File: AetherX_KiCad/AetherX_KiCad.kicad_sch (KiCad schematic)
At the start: 17 parts, among them J1 SWD Connector, SW1 SW_SPDT, U1 STM32F401RETx, Y1 8MHz

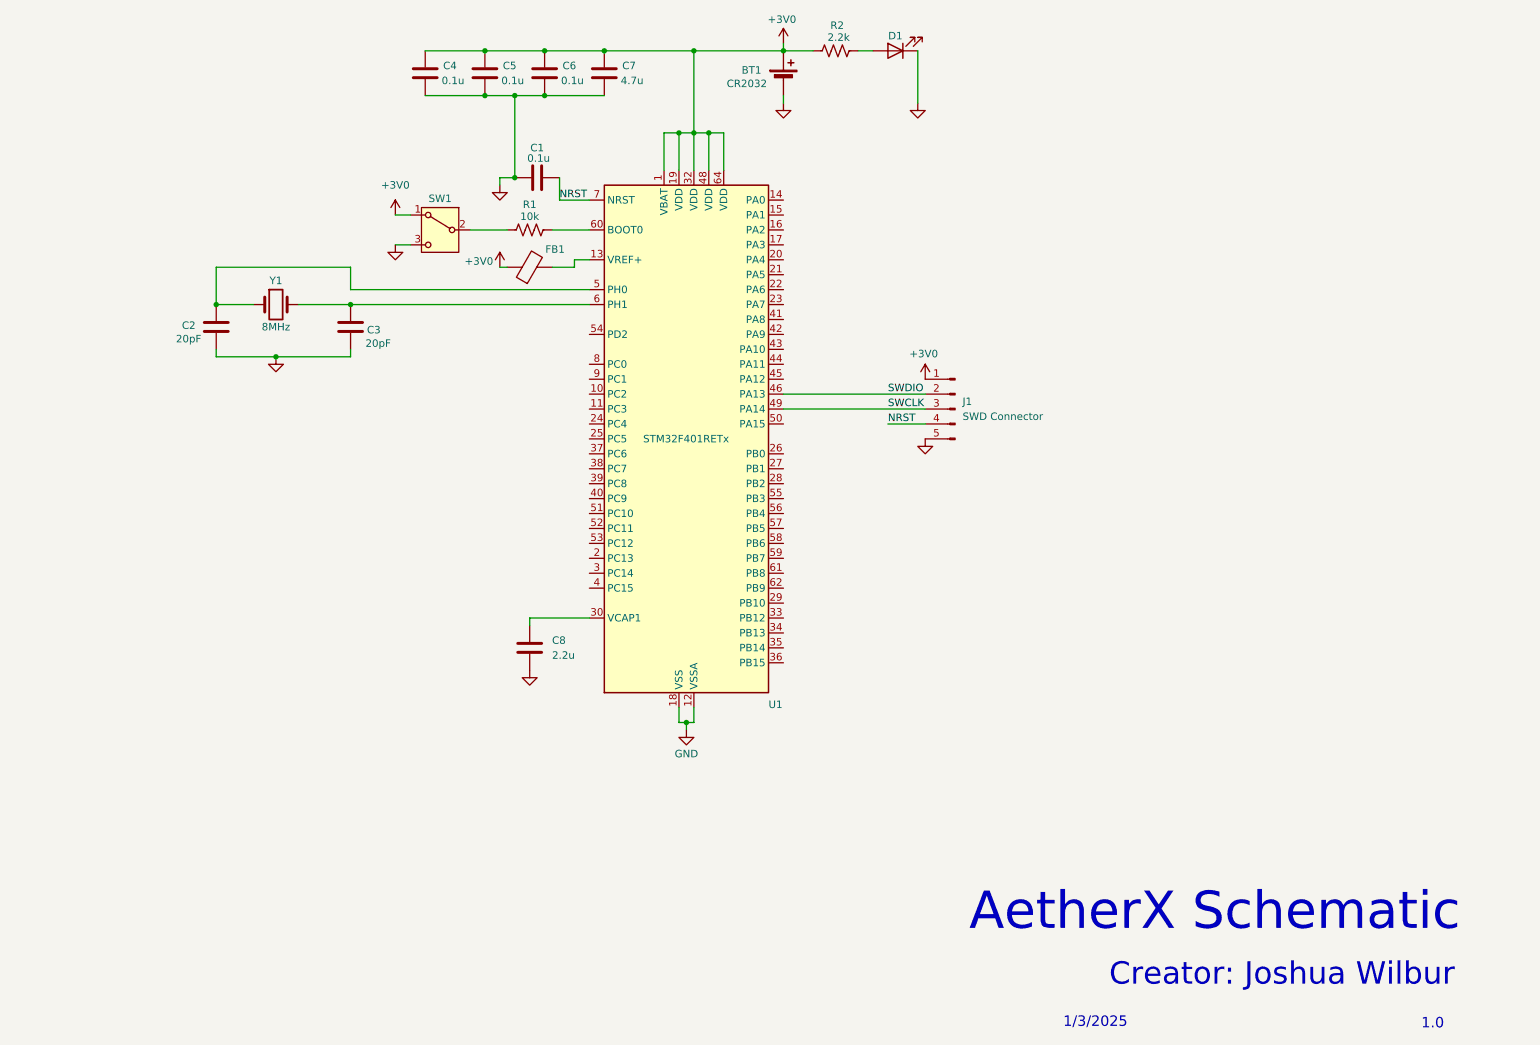
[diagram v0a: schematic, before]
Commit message: update schematic
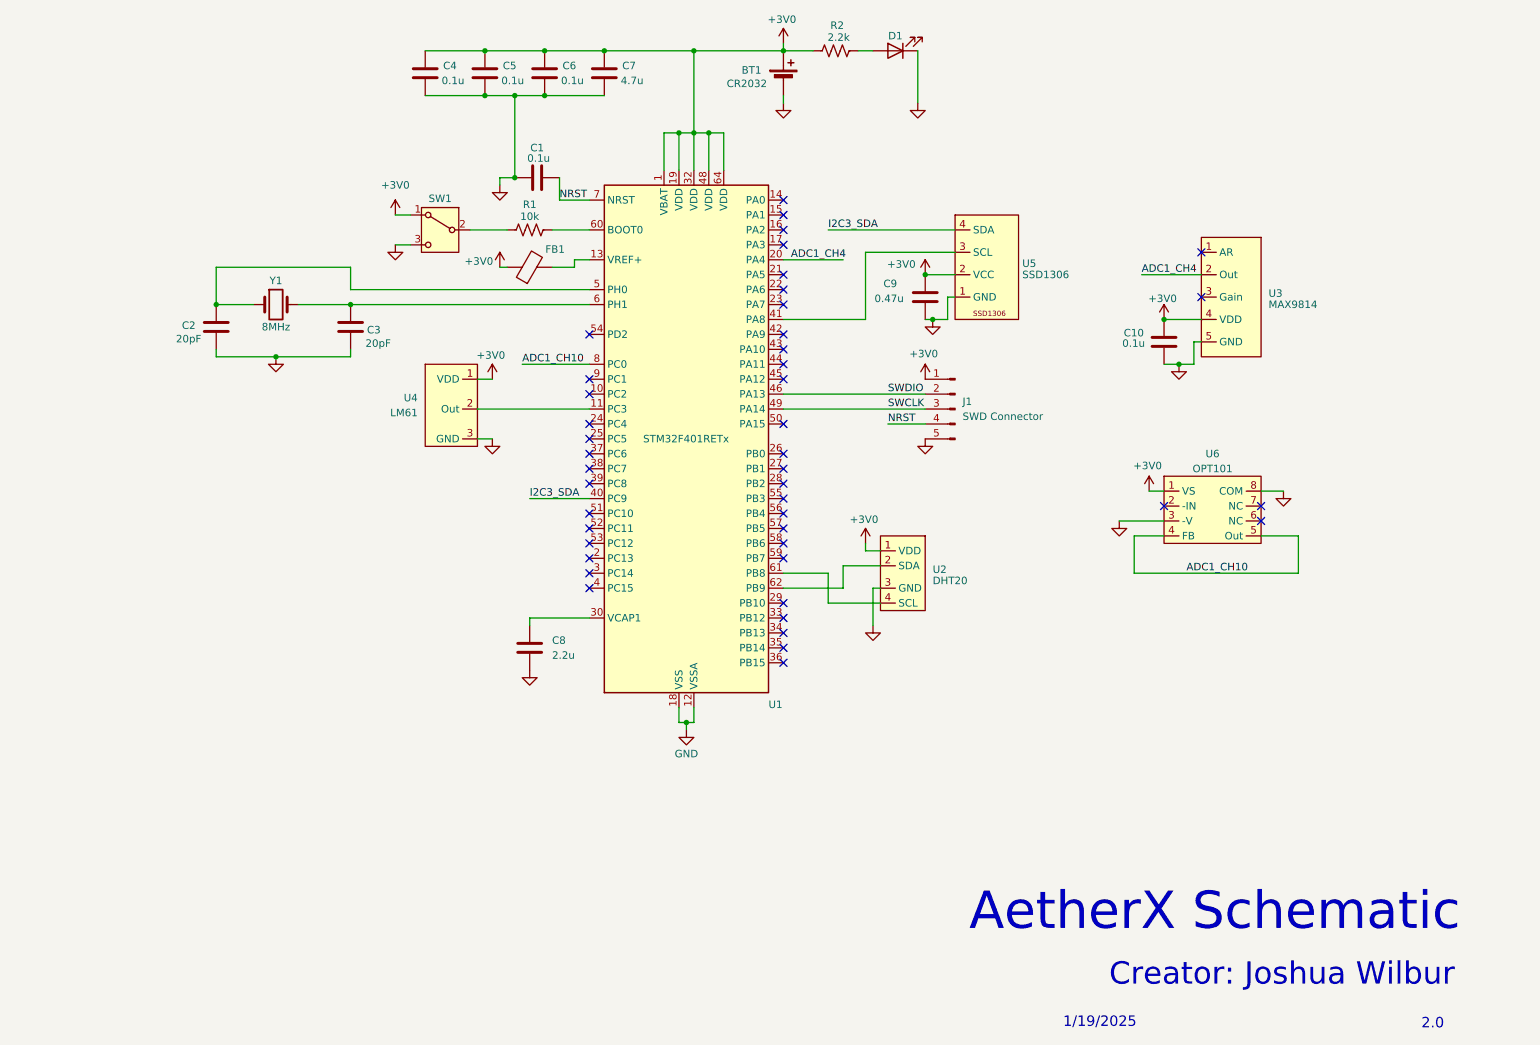
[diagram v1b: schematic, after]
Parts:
- added C10: 0.1u, symbol Device:C
- added C9: 0.47u, symbol Device:C
- added U2: DHT20, symbol Device:DHT20
- added U3: MAX9814, symbol Device:MAX9814
- added U4: LM61, symbol Device:LM61
- added U5: SSD1306, symbol Device:SSD1306_LCD
- added U6: OPT101, symbol Device:OPT101
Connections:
- net +3V0: now also C10.1, C9.1, U2.1 (VDD), U3.4 (VDD), U4.1 (VDD), U5.2 (VCC), U6.1 (VS)
- net GND: now also C10.2, C9.2, U2.3 (GND), U3.5 (GND), U4.3 (GND), U5.1 (GND), U6.3 (-V), U6.8 (COM)
- net at U1.11 (PC3): now also U4.2 (Out)
- net ADC1_CH4: now reaches U1.20 (PA4)
- net ADC1_CH4: now also U3.2 (Out)
- net I2C3_SDA: now reaches U1.40 (PC9)
- net I2C3_SDA: now also U5.4 (SDA)
- net at U1.41 (PA8): now also U5.3 (SCL)
- net at U1.61 (PB8): now also U2.4 (SCL)
- net at U1.62 (PB9): now also U2.2 (SDA)
- net ADC1_CH10: now reaches U1.8 (PC0)
- net ADC1_CH10: now also U6.4 (FB), U6.5 (Out)
- no-connect marks 0 -> 44
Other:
- note added: "1/19/2025"
- note added: "2.0"
- note removed: "1.0"
- note removed: "1/3/2025"

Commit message: internal ADC VRef code added
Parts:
- added C11, C12: 0.1u, symbol Device:C
- added R3, R5: 1k, symbol Device:R_US
- added R4, R6: 10k, symbol Device:R_US
- added SW2, SW3: SW_Push, symbol Switch:SW_Push
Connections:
- net +3V0: now also R4.1, R6.1
- net GND: now also C11.2, C12.2, SW2.1, SW3.1
- net Button1: now reaches U1.24 (PC4)
- net Button1: now also C11.1, R3.2, R4.2
- net Button2: now reaches U1.25 (PC5)
- net Button2: now also C12.1, R5.2, R6.2
- new net: R5.1, SW3.2
- new net: R3.1, SW2.2
- no-connect marks 44 -> 42

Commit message: schematic V2 complete
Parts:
- added C13: 0.1u, Capacitor_SMD:C_0402_1005Metric_Pad0.74x0.62mm_HandSolder, symbol Device:C
- BT1: footprint (none) -> Battery:BatteryHolder_Keystone_103_1x20mm; now left out of the parts list
- C1, C2, C3, Y1: now left out of the parts list
- C10, C11, C12: footprint (none) -> Capacitor_SMD:C_0402_1005Metric_Pad0.74x0.62mm_HandSolder
- C8, C9: footprint (none) -> Capacitor_THT:C_Disc_D5.1mm_W3.2mm_P5.00mm; now left out of the parts list
- D1: footprint (none) -> LED_THT:LED_D5.0mm; now left out of the parts list
- FB1: footprint (none) -> Inductor_THT:L_Axial_L7.0mm_D3.3mm_P12.70mm_Horizontal_Fastron_MICC
- J1, U3: footprint (none) -> Connector_PinSocket_2.54mm:PinSocket_1x05_P2.54mm_Vertical; now left out of the parts list
- R1, R2, R4, R6: footprint (none) -> Resistor_THT:R_Axial_DIN0207_L6.3mm_D2.5mm_P10.16mm_Horizontal; now left out of the parts list
- R3, R5: footprint (none) -> Resistor_THT:R_Axial_DIN0207_L6.3mm_D2.5mm_P10.16mm_Horizontal
- SW1, U4: footprint (none) -> Connector_PinHeader_2.54mm:PinHeader_1x03_P2.54mm_Vertical; now left out of the parts list
- SW2, SW3: footprint (none) -> Button_Switch_THT:SW_PUSH_1P1T_6x3.5mm_H5.0_APEM_MJTP1250; now left out of the parts list
- U2, U5: footprint (none) -> Connector_PinSocket_2.54mm:PinSocket_1x04_P2.54mm_Vertical; now left out of the parts list
- U6: footprint (none) -> Package_DIP:DIP-8_W7.62mm; now left out of the parts list
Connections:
- net +3V0: now also C13.1
- net GND: now also C13.2
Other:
- note added: "1/30/2025"
- note added: "2.2"
- note removed: "1/19/2025"
- note removed: "2.0"
- moved on the sheet: C11, C12, R3, R4, R5, R6, SW2, SW3

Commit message: first PCB complete
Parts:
- renumbered SW2 to SW1, SW3 to SW2, SW1 to SW_BOOT1
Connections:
- net +3V0: no longer R2.1
- net LED: now reaches U1.51 (PC10)
- net LED: now also R2.1
- no-connect marks 42 -> 41
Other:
- moved on the sheet: D1, R2
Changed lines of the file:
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@@
 	)
 	(no_connect
-		(at 127 106.68)
-	)
-	(no_connect
 		(at 160.02 101.6)
 	)
@@
 	(wire
 		(pts
-			(xy 160.02 27.94) (xy 165.1 27.94)
-		)
-		(stroke
-			(width 0)
-			(type default)
-		)
-	)
-	(wire
-		(pts
 			(xy 142.24 41.91) (xy 144.78 41.91)
 		)
@@
 	(wire
 		(pts
+			(xy 175.26 36.83) (xy 180.34 36.83)
+		)
+		(stroke
+			(width 0)
+			(type default)
+		)
+	)
+	(wire
+		(pts
 			(xy 120.65 58.42) (xy 127 58.42)
 		)
@@
 	(wire
 		(pts
-			(xy 172.72 27.94) (xy 175.26 27.94)
+			(xy 187.96 36.83) (xy 190.5 36.83)
 		)
 		(stroke
@@
 	(wire
 		(pts
+			(xy 116.84 106.68) (xy 127 106.68)
+		)
+		(stroke
+			(width 0)
+			(type default)
+		)
+	)
+	(wire
+		(pts
 			(xy 167.64 121.92) (xy 176.53 121.92)
 		)
@@
 	(wire
 		(pts
-			(xy 182.88 27.94) (xy 182.88 36.83)
+			(xy 198.12 36.83) (xy 198.12 45.72)
 		)
 		(stroke
@@
 		)
 	)
+	(label "LED"
+		(at 116.84 106.68 0)
+		(effects
+			(font
+				(size 1.27 1.27)
+			)
+			(justify left bottom)
+		)
+	)
 	(label "ADC1_CH4"
 		(at 161.29 63.5 0)
@@
 		)
 	)
+	(label "LED"
+		(at 175.26 36.83 0)
+		(effects
+			(font
+				(size 1.27 1.27)
+			)
+			(justify left bottom)
+		)
+	)
 	(label "SWDIO"
 		(at 177.8 86.36 0)
@@
 		(on_board yes)
 		(dnp no)
-		(property "Reference" "SW1"
+		(property "Reference" "SW_BOOT1"
 			(at 101.6 53.086 0)
 			(effects
@@
 			(project ""
 				(path "/e3a9a061-ed84-4419-81aa-dfe9405e0b6b"
-					(reference "SW1")
+					(reference "SW_BOOT1")
 					(unit 1)
 				)
@@
 	(symbol
 		(lib_id "power:GND")
-		(at 182.88 36.83 0)
+		(at 198.12 45.72 0)
 		(unit 1)
 		(exclude_from_sim no)
@@
 		(fields_autoplaced yes)
 		(property "Reference" "#PWR08"
-			(at 182.88 43.18 0)
+			(at 198.12 52.07 0)
 			(effects
 				(font
@@
 		)
 		(property "Value" "GND"
-			(at 182.88 41.91 0)
+			(at 198.12 50.8 0)
 			(effects
 				(font
@@
 		)
 		(property "Footprint" ""
-			(at 182.88 36.83 0)
+			(at 198.12 45.72 0)
 			(effects
 				(font
@@
 		)
 		(property "Datasheet" ""
-			(at 182.88 36.83 0)
+			(at 198.12 45.72 0)
 			(effects
 				(font
@@
 		)
 		(property "Description" "Power symbol creates a global label with name \"GND\" , ground"
-			(at 182.88 36.83 0)
+			(at 198.12 45.72 0)
 			(effects
 				(font
@@
 	(symbol
 		(lib_id "Device:R_US")
-		(at 168.91 27.94 90)
+		(at 184.15 36.83 90)
 		(unit 1)
 		(exclude_from_sim no)
@@
 		(dnp no)
 		(property "Reference" "R2"
-			(at 169.164 23.622 90)
+			(at 184.404 32.512 90)
 			(effects
 				(font
@@
 		)
 		(property "Value" "2.2k"
-			(at 169.418 25.654 90)
+			(at 184.658 34.544 90)
 			(effects
 				(font
@@
 		)
 		(property "Footprint" "Resistor_THT:R_Axial_DIN0207_L6.3mm_D2.5mm_P10.16mm_Horizontal"
-			(at 169.164 26.924 90)
+			(at 184.404 35.814 90)
 			(effects
 				(font
@@
 		)
 		(property "Datasheet" "~"
-			(at 168.91 27.94 0)
+			(at 184.15 36.83 0)
 			(effects
 				(font
@@
 		)
 		(property "Description" "Resistor, US symbol"
-			(at 168.91 27.94 0)
+			(at 184.15 36.83 0)
 			(effects
 				(font
@@
 	(symbol
 		(lib_id "Device:LED")
-		(at 179.07 27.94 180)
+		(at 194.31 36.83 180)
 		(unit 1)
 		(exclude_from_sim no)
@@
 		(dnp no)
 		(property "Reference" "D1"
-			(at 179.07 25.4 0)
+			(at 194.31 34.29 0)
 			(effects
 				(font
@@
 		)
 		(property "Value" "LED"
-			(at 179.324 25.4 0)
+			(at 194.564 34.29 0)
 			(effects
 				(font
@@
 		)
 		(property "Footprint" "LED_THT:LED_D5.0mm"
-			(at 179.07 27.94 0)
+			(at 194.31 36.83 0)
 			(effects
 				(font
@@
 		)
 		(property "Datasheet" "~"
-			(at 179.07 27.94 0)
+			(at 194.31 36.83 0)
 			(effects
 				(font
@@
 		)
 		(property "Description" "Light emitting diode"
-			(at 179.07 27.94 0)
+			(at 194.31 36.83 0)
 			(effects
 				(font
@@
 		(dnp no)
 		(fields_autoplaced yes)
-		(property "Reference" "SW2"
+		(property "Reference" "SW1"
 			(at 33.02 114.2999 90)
 			(effects
@@
 			(project ""
 				(path "/e3a9a061-ed84-4419-81aa-dfe9405e0b6b"
-					(reference "SW2")
+					(reference "SW1")
 					(unit 1)
 				)
@@
 		(dnp no)
 		(fields_autoplaced yes)
-		(property "Reference" "SW3"
+		(property "Reference" "SW2"
 			(at 33.02 149.8599 90)
 			(effects
@@
 			(project "AetherX_KiCad"
 				(path "/e3a9a061-ed84-4419-81aa-dfe9405e0b6b"
-					(reference "SW3")
+					(reference "SW2")
 					(unit 1)
 				)

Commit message: PCB ordered, uploaded BOM and gerber files
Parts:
- R3, R5: now left out of the parts list
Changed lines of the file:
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@@
 		(unit 1)
 		(exclude_from_sim no)
-		(in_bom yes)
+		(in_bom no)
 		(on_board yes)
 		(dnp no)
@@
 		(unit 1)
 		(exclude_from_sim no)
-		(in_bom yes)
-		(on_board yes)
-		(dnp no)
+		(in_bom no)
+		(on_board yes)
+		(dnp no)

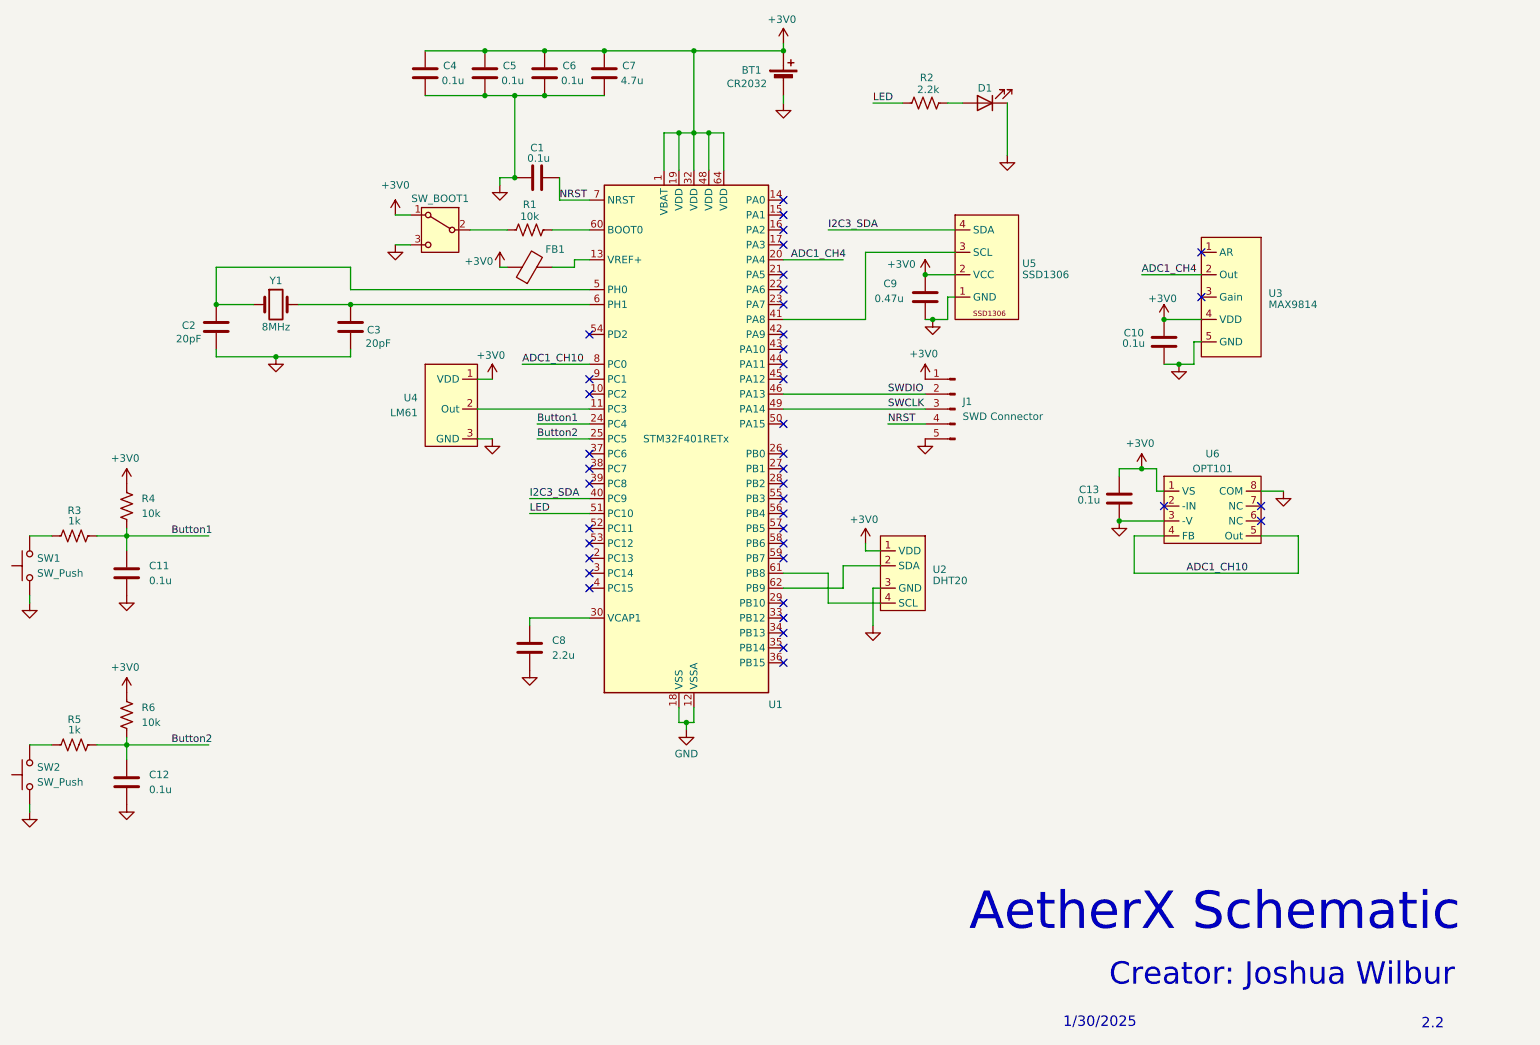
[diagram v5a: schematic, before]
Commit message: schematic v3 uploaded
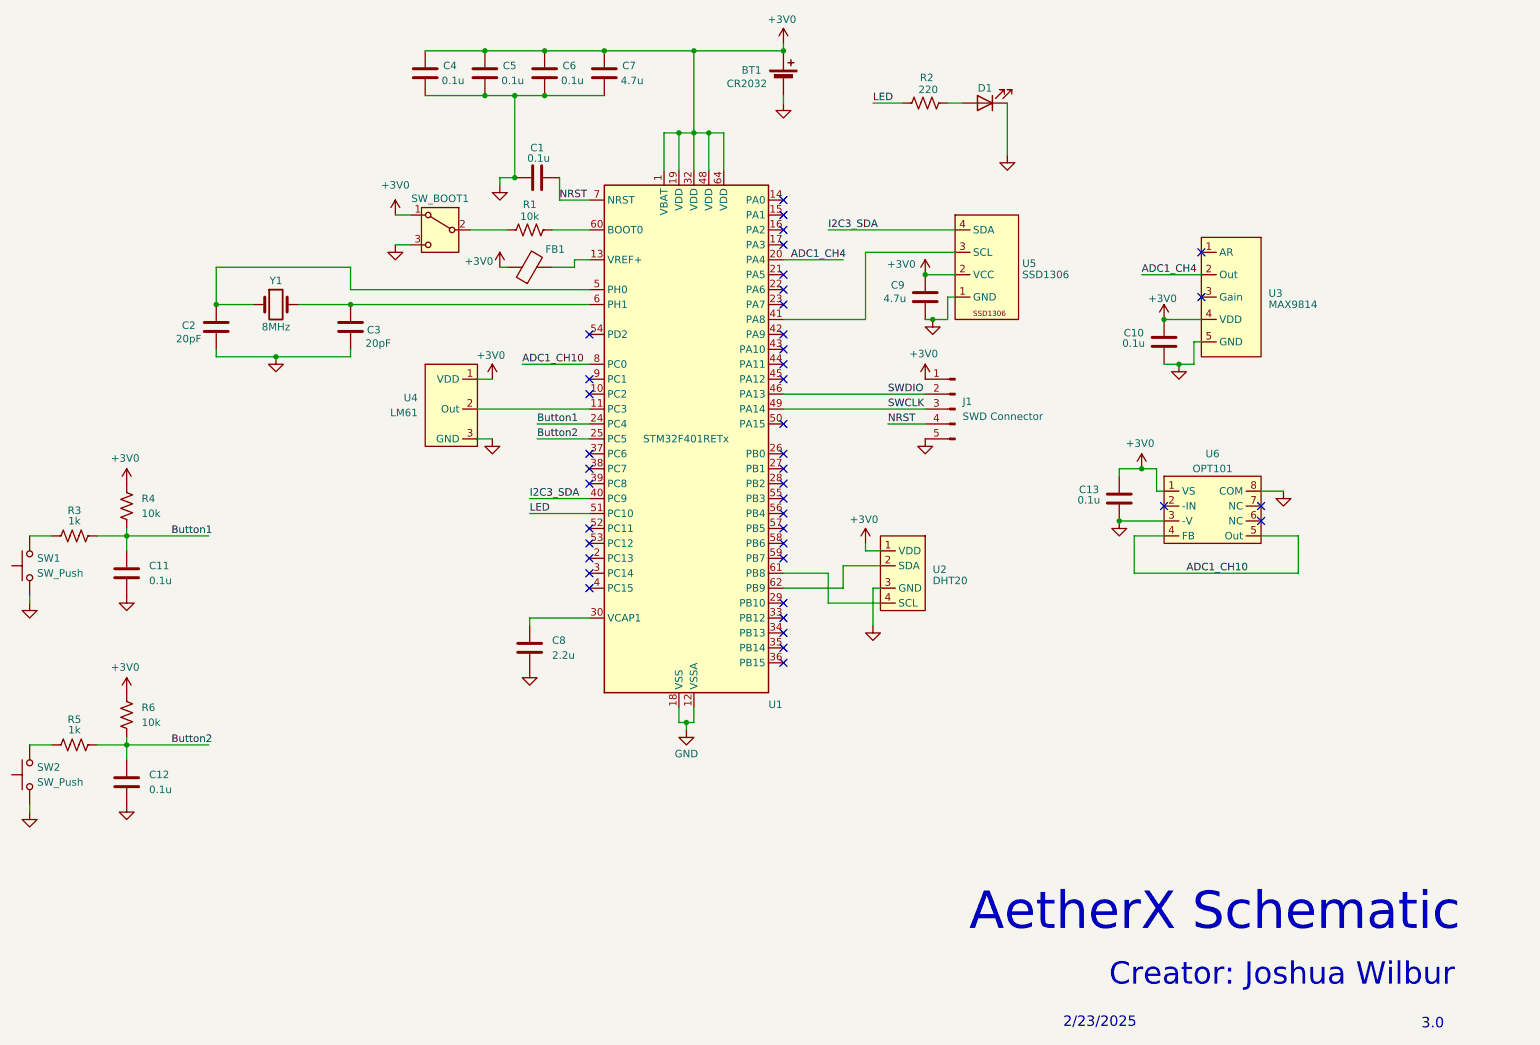
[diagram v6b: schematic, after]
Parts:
- C9: value 0.47u -> 4.7u
- R2: value 2.2k -> 220
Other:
- note added: "2/23/2025"
- note added: "3.0"
- note removed: "1/30/2025"
- note removed: "2.2"
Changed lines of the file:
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@@
 		)
 	)
-	(text "2.2"
+	(text "3.0"
 		(exclude_from_sim no)
 		(at 270.51 193.548 0)
@@
 		)
 	)
-	(text "1/30/2025"
+	(text "2/23/2025"
 		(exclude_from_sim no)
 		(at 213.868 193.294 0)
@@
 			)
 		)
-		(property "Value" "2.2k"
+		(property "Value" "220"
 			(at 184.658 34.544 90)
 			(effects
@@
 		(dnp no)
 		(property "Reference" "C9"
-			(at 177.038 67.564 0)
+			(at 178.308 67.818 0)
 			(effects
 				(font
@@
 			)
 		)
-		(property "Value" "0.47u"
-			(at 175.514 70.104 0)
-			(effects
-				(font
+		(property "Value" "4.7u"
+			(at 177.038 70.104 0)
+			(effects
+				(font
